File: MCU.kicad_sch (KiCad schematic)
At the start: 32 parts, among them J4 2125281600, J5 Conn_02x08_Odd_Even, J6 Conn_02x08_Odd_Even, U7 STM32F405RGTx, Y1 8MHz

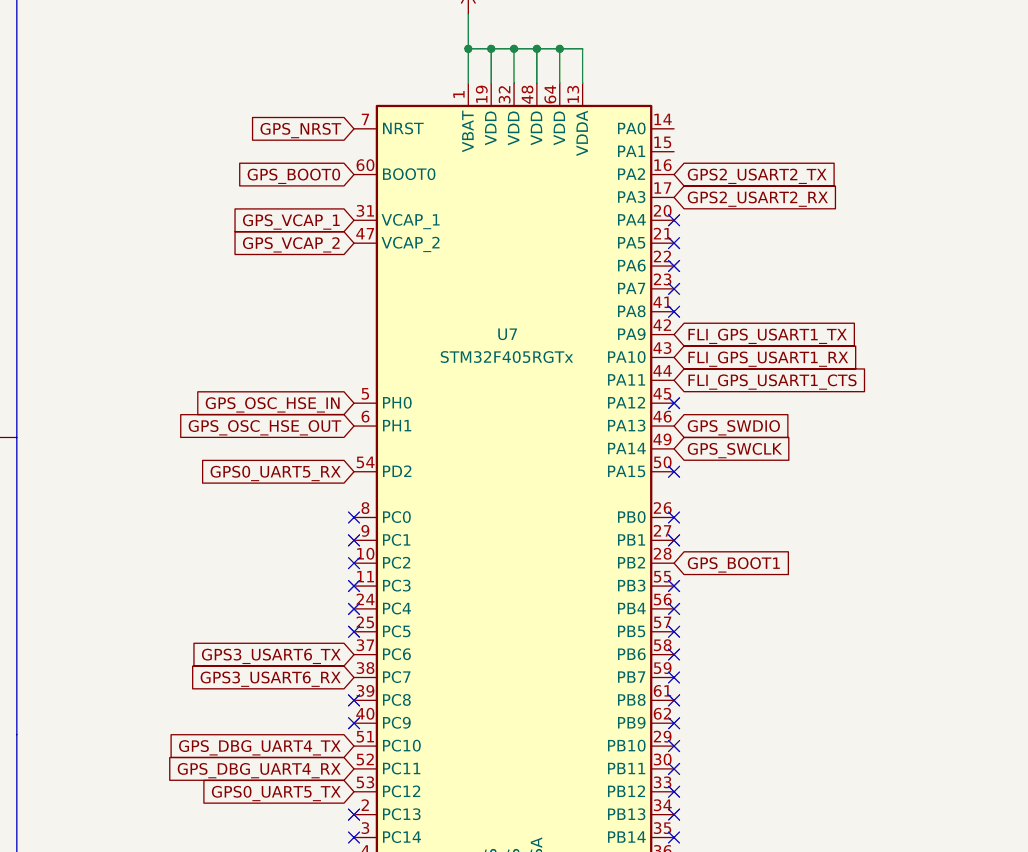
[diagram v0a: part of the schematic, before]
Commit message: Adding M10
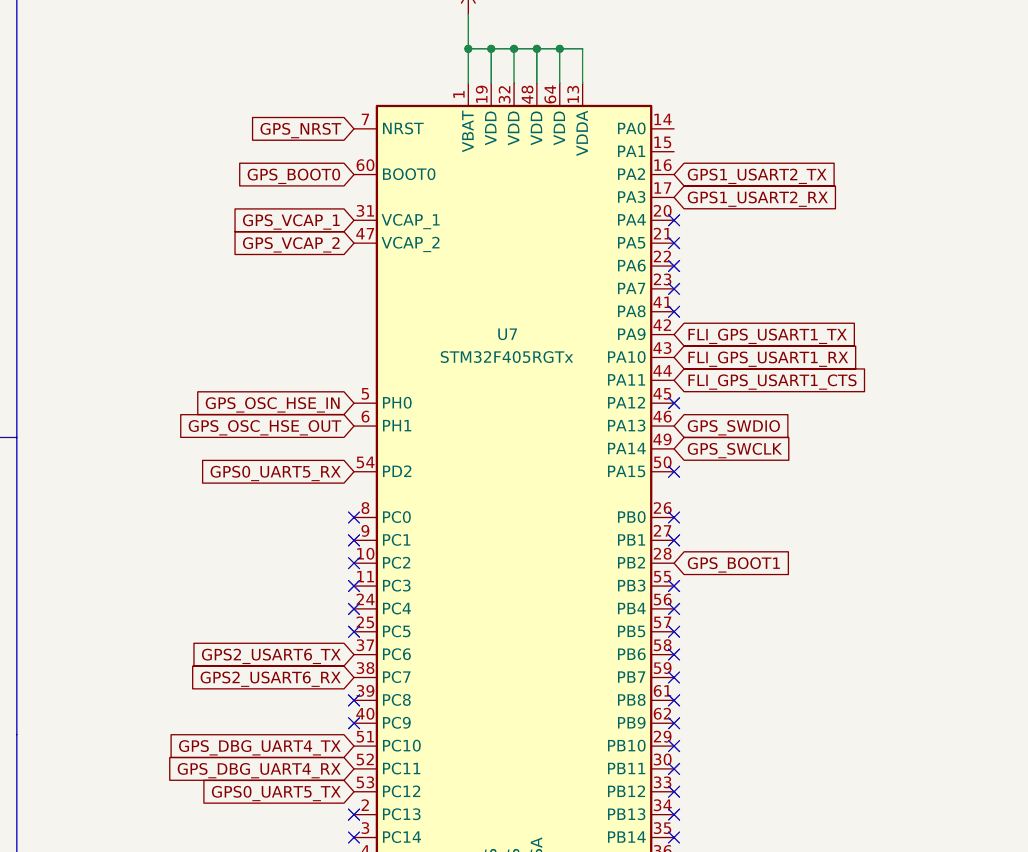
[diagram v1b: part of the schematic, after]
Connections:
- net GPS2_USART2_RX renamed GPS1_USART2_RX
- net GPS2_USART2_TX renamed GPS1_USART2_TX
- net GPS3_USART6_RX renamed GPS2_USART6_RX
- net GPS3_USART6_TX renamed GPS2_USART6_TX
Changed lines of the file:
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@@
     )
   )
-  (global_label "GPS2_USART2_TX" (shape input) (at 139.7 86.36 0) (fields_autoplaced)
+  (global_label "GPS1_USART2_TX" (shape input) (at 139.7 86.36 0) (fields_autoplaced)
     (effects (font (size 1.27 1.27)) (justify left))
     (property "Intersheet References" "${INTERSHEET_REFS}" (id 0) (at 158.2602 86.2806 0)
@@
     )
   )
-  (global_label "GPS3_USART6_TX" (shape input) (at 104.14 139.7 180) (fields_autoplaced)
+  (global_label "GPS2_USART6_TX" (shape input) (at 104.14 139.7 180) (fields_autoplaced)
     (effects (font (size 1.27 1.27)) (justify right))
     (property "Intersheet References" "${INTERSHEET_REFS}" (id 0) (at 85.5798 139.6206 0)
@@
     )
   )
-  (global_label "GPS3_USART6_RX" (shape input) (at 104.14 142.24 180) (fields_autoplaced)
+  (global_label "GPS2_USART6_RX" (shape input) (at 104.14 142.24 180) (fields_autoplaced)
     (effects (font (size 1.27 1.27)) (justify right))
     (property "Intersheet References" "${INTERSHEET_REFS}" (id 0) (at 85.2774 142.1606 0)
@@
     )
   )
-  (global_label "GPS2_USART2_RX" (shape input) (at 139.7 88.9 0) (fields_autoplaced)
+  (global_label "GPS1_USART2_RX" (shape input) (at 139.7 88.9 0) (fields_autoplaced)
     (effects (font (size 1.27 1.27)) (justify left))
     (property "Intersheet References" "${INTERSHEET_REFS}" (id 0) (at 158.5626 88.8206 0)

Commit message: Finished M10
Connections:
- net GPS3_RESET: now reaches U7.15 (PA1)
- net GPS1_RESET: now reaches U7.23 (PA7)
- net GPS1_USART3_TX: now reaches U7.29 (PB10)
- net GPS1_USART3_RX: now reaches U7.30 (PB11)
- net GPS2_RESET: now reaches U7.34 (PB13)
- net GPS0_RESET: now reaches U7.55 (PB3)
- net GPS1_USART2_RX renamed GPS3_USART2_RX
- net GPS1_USART2_TX renamed GPS3_USART2_TX
- no-connect marks 40 -> 36
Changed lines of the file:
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@@
   (no_connect (at 139.7 127))
   (no_connect (at 219.71 97.79))
-  (no_connect (at 139.7 99.06))
   (no_connect (at 104.14 147.32))
   (no_connect (at 139.7 101.6))
@@
   (no_connect (at 139.7 137.16))
   (no_connect (at 139.7 119.38))
-  (no_connect (at 139.7 152.4))
   (no_connect (at 104.14 134.62))
   (no_connect (at 245.11 100.33))
@@
   (no_connect (at 245.11 97.79))
   (no_connect (at 104.14 132.08))
+  (no_connect (at 139.7 81.28))
   (no_connect (at 219.71 100.33))
   (no_connect (at 139.7 154.94))
   (no_connect (at 139.7 160.02))
   (no_connect (at 245.11 95.25))
-  (no_connect (at 139.7 149.86))
   (no_connect (at 139.7 96.52))
   (no_connect (at 104.14 137.16))
-  (no_connect (at 139.7 132.08))
-  (no_connect (at 139.7 157.48))
   (no_connect (at 104.14 144.78))
   (no_connect (at 104.14 124.46))
@@
     )
   )
+  (global_label "GPS2_RESET" (shape input) (at 139.7 157.48 0) (fields_autoplaced)
+    (effects (font (size 1.27 1.27)) (justify left))
+    (property "Intersheet References" "${INTERSHEET_REFS}" (id 0) (at 153.785 157.4006 0)
+      (effects (font (size 1.27 1.27)) (justify left) hide)
+    )
+  )
   (global_label "GPS_NRST" (shape input) (at 219.71 107.95 180) (fields_autoplaced)
     (effects (font (size 1.27 1.27)) (justify right))
@@
     )
   )
+  (global_label "GPS1_USART3_RX" (shape input) (at 139.7 152.4 0) (fields_autoplaced)
+    (effects (font (size 1.27 1.27)) (justify left))
+    (property "Intersheet References" "${INTERSHEET_REFS}" (id 0) (at 158.5626 152.3206 0)
+      (effects (font (size 1.27 1.27)) (justify left) hide)
+    )
+  )
   (global_label "GPS_BOOT1" (shape input) (at 40.005 44.45 180) (fields_autoplaced)
     (effects (font (size 1.27 1.27)) (justify right))
@@
     (property "Intersheet References" "${INTERSHEET_REFS}" (id 0) (at 198.4888 105.3306 0)
       (effects (font (size 1.27 1.27)) (justify right) hide)
+    )
+  )
+  (global_label "GPS3_RESET" (shape input) (at 139.7 83.82 0) (fields_autoplaced)
+    (effects (font (size 1.27 1.27)) (justify left))
+    (property "Intersheet References" "${INTERSHEET_REFS}" (id 0) (at 153.785 83.7406 0)
+      (effects (font (size 1.27 1.27)) (justify left) hide)
     )
   )
@@
     )
   )
-  (global_label "GPS1_USART2_TX" (shape input) (at 139.7 86.36 0) (fields_autoplaced)
+  (global_label "GPS3_USART2_TX" (shape input) (at 139.7 86.36 0) (fields_autoplaced)
     (effects (font (size 1.27 1.27)) (justify left))
     (property "Intersheet References" "${INTERSHEET_REFS}" (id 0) (at 158.2602 86.2806 0)
@@
     )
   )
+  (global_label "GPS1_RESET" (shape input) (at 139.7 99.06 0) (fields_autoplaced)
+    (effects (font (size 1.27 1.27)) (justify left))
+    (property "Intersheet References" "${INTERSHEET_REFS}" (id 0) (at 153.785 98.9806 0)
+      (effects (font (size 1.27 1.27)) (justify left) hide)
+    )
+  )
   (global_label "GPS_OSC_HSE_IN" (shape input) (at 60.325 199.39 0) (fields_autoplaced)
     (effects (font (size 1.27 1.27)) (justify left))
@@
     )
   )
+  (global_label "GPS1_USART3_TX" (shape input) (at 139.7 149.86 0) (fields_autoplaced)
+    (effects (font (size 1.27 1.27)) (justify left))
+    (property "Intersheet References" "${INTERSHEET_REFS}" (id 0) (at 158.2602 149.7806 0)
+      (effects (font (size 1.27 1.27)) (justify left) hide)
+    )
+  )
   (global_label "GPS_BOOT0" (shape input) (at 104.14 86.36 180) (fields_autoplaced)
     (effects (font (size 1.27 1.27)) (justify right))
@@
     )
   )
+  (global_label "GPS0_RESET" (shape input) (at 139.7 132.08 0) (fields_autoplaced)
+    (effects (font (size 1.27 1.27)) (justify left))
+    (property "Intersheet References" "${INTERSHEET_REFS}" (id 0) (at 153.785 132.0006 0)
+      (effects (font (size 1.27 1.27)) (justify left) hide)
+    )
+  )
   (global_label "GPS_DBG_UART4_TX" (shape input) (at 219.71 102.87 180) (fields_autoplaced)
     (effects (font (size 1.27 1.27)) (justify right))
@@
     )
   )
-  (global_label "GPS1_USART2_RX" (shape input) (at 139.7 88.9 0) (fields_autoplaced)
+  (global_label "GPS3_USART2_RX" (shape input) (at 139.7 88.9 0) (fields_autoplaced)
     (effects (font (size 1.27 1.27)) (justify left))
     (property "Intersheet References" "${INTERSHEET_REFS}" (id 0) (at 158.5626 88.8206 0)

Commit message: Last commit
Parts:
- added TP4: TestPoint, TestPoint:TestPoint_Pad_D1.0mm, symbol Connector:TestPoint
- C12: value 1uF -> 100nF
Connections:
- net GND: now also TP4.1
- net GPS_DBG_UART4_RX: now also J4.5; no longer J4.6
- net GPS_DBG_UART4_TX: now also J4.6; no longer J4.5
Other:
- moved on the sheet: TP1, TP2, TP3

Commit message: Second commit
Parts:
- removed JP1: SJumper, Jumper:SolderJumper-2_P1.3mm_Open_TrianglePad1.0x1.5mm, symbol Jumper:SolderJumper_2_Open
- added C28: 1uF, Capacitor_SMD:C_0402_1005Metric, symbol Device:C_Small
- added U5: SN74LV4052APWR, SN74LV4052APWR:PW16, symbol 2026-03-05_10-17-03:SN74LV4052APWR
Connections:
- net +3.3V: now also C28.1, U5.16 (VCC)
- net GND: now also C28.2, U5.7 (GND), U5.8 (GND)
- net GPS0_RESET: now also U7.57 (PB5); no longer U7.55 (PB3)
- net GPS0_UART5_RX: now also U5.12 (1Y0)
- net GPS0_UART5_TX: now also U5.1 (2Y0)
- net GPS1_RESET: now also U7.26 (PB0); no longer U7.23 (PA7)
- net GPS2_RESET: now also U7.39 (PC8); no longer U7.34 (PB13)
- net GPS2_USART6_RX: now also U5.11 (1Y3)
- net GPS2_USART6_TX: now also U5.4 (2Y3)
- net GPS_MUX_UART_RX: now reaches J4.10
- net GPS_MUX_UART_RX: now also U5.13 (1-COM)
- net GPS_MUX_UART_TX: now reaches J4.11
- net GPS_MUX_UART_TX: now also U5.3 (2-COM)
- net GPS_MUX_A: now reaches U7.59 (PB7)
- net GPS_MUX_A: now also U5.10 (A)
- net GPS_MUX_B: now reaches U7.61 (PB8)
- net GPS_MUX_B: now also U5.9 (B)
- net GPS_MUX_INH: now reaches U7.62 (PB9)
- net GPS_MUX_INH: now also U5.6 (INH)
- net GPS1_USART3_RX: no longer names the net of U7.30 (PB11)
- net GPS1_USART3_TX: no longer names the net of U7.29 (PB10)
- net GPS3_RESET: no longer names the net of U7.15 (PA1)
- net GPS3_USART2_RX renamed GPS1_USART2_RX
- net GPS1_USART2_RX: now also U5.14 (1Y1)
- net GPS3_USART2_TX renamed GPS1_USART2_TX
- net GPS1_USART2_TX: now also U5.5 (2Y1)
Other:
- moved on the sheet: C10, C11, C12, C13, C14, C15, C16, C17, C18, C19, C20, C21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

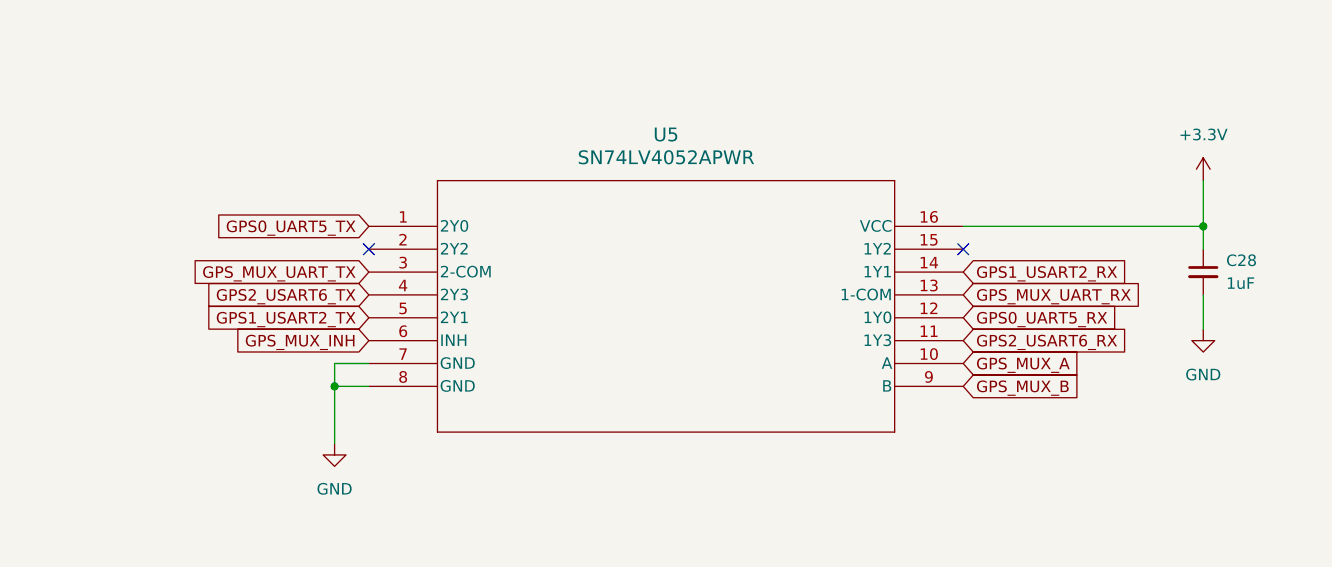
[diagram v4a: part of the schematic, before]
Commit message: Correcet MUX pins
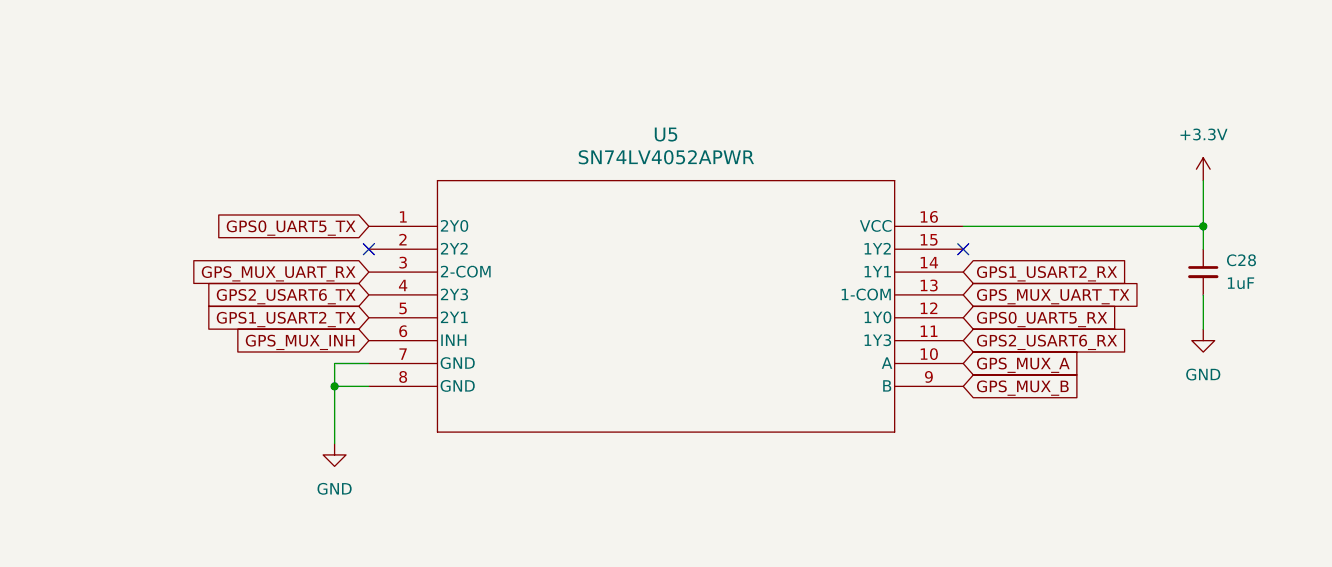
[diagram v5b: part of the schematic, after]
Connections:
- net GPS_MUX_UART_RX: now also U5.3 (2-COM); no longer U5.13 (1-COM)
- net GPS_MUX_UART_TX: now also U5.13 (1-COM); no longer U5.3 (2-COM)
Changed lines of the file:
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@@
 	(global_label "GPS_MUX_UART_RX"
+		(shape input)
+		(at 284.48 93.98 180)
+		(fields_autoplaced yes)
+		(effects
+			(font
+				(size 1.27 1.27)
+			)
+			(justify right)
+		)
+		(property "Intersheetrefs" "${INTERSHEET_REFS}"
+			(at 263.7149 93.98 0)
+			(effects
+				(font
+					(size 1.27 1.27)
+				)
+				(justify right)
+				(hide yes)
+			)
+		)
+	)
+	(global_label "GPS_MUX_UART_TX"
 		(shape input)
 		(at 350.52 96.52 0)
@@
 		)
 		(property "Intersheetrefs" "${INTERSHEET_REFS}"
-			(at 371.2851 96.52 0)
+			(at 370.9827 96.52 0)
 			(effects
 				(font
@@
 				(hide yes)
 			)
-		)
-	)
-	(global_label "GPS_MUX_UART_TX"
-		(shape input)
-		(at 284.48 93.98 180)
-		(fields_autoplaced yes)
-		(effects
-			(font
-				(size 1.27 1.27)
-			)
-			(justify right)
-		)
-		(property "Intersheetrefs" "${INTERSHEET_REFS}"
-			(at 264.0173 93.98 0)
-			(effects
-				(font
-					(size 1.27 1.27)
-				)
-				(justify right)
-				(hide yes)
-			)
